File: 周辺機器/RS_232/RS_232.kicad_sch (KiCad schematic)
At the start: 16 parts, among them SW1 SW_DIP_x04, U1 CD74HC08, U10 74HC595, U11 74LS195, U2 CD74HC04, U3 4020, U4 4040, U5 74HC74, U6 74LS195, U7 74HC74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

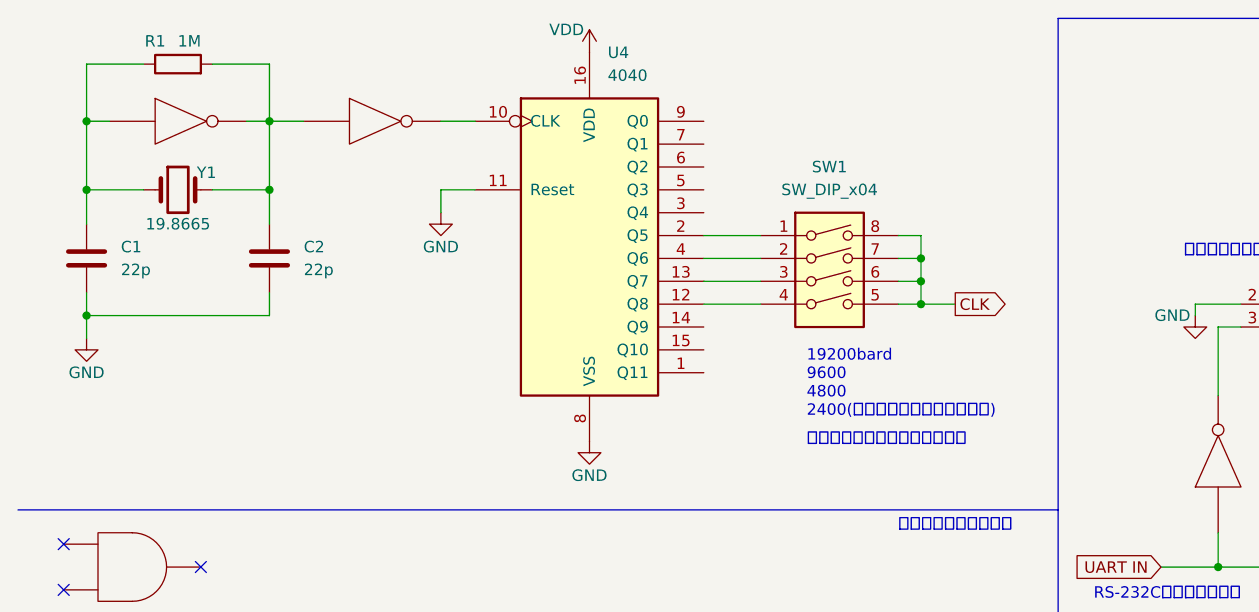
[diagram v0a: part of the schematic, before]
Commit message: 周辺機器RS-232C,定数および接続ピンの修正
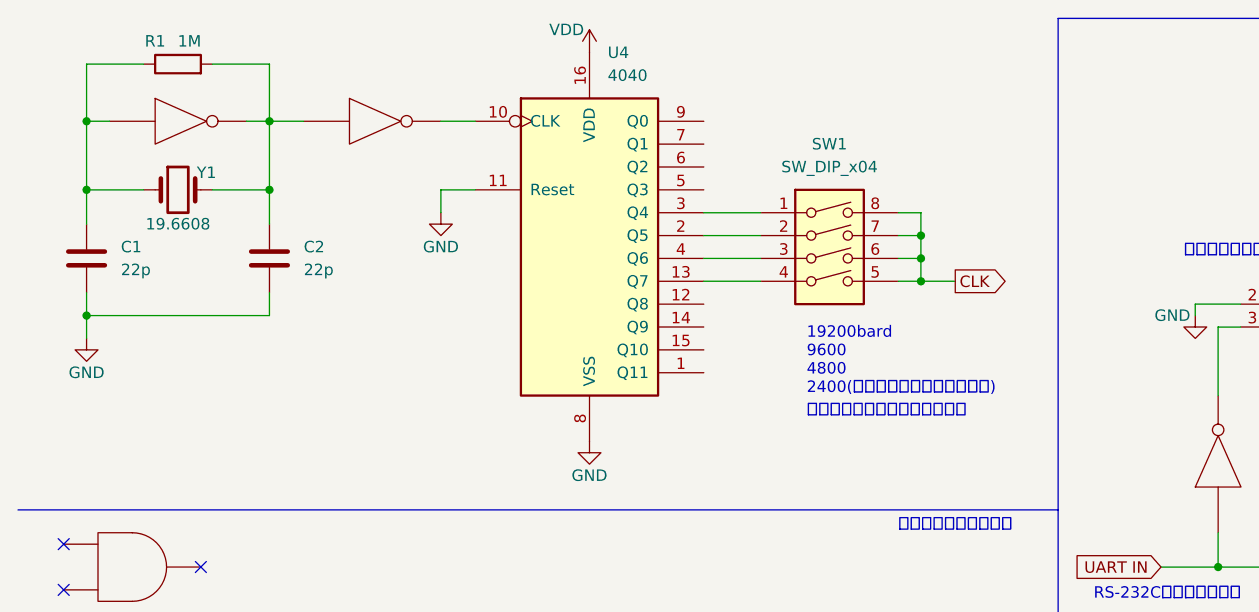
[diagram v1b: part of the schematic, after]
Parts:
- Y1: value 19.8665 -> 19.6608
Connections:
- net at SW1.1: now also U4.3 (Q4); no longer U4.2 (Q5)
- net at SW1.2: now also U4.2 (Q5); no longer U4.4 (Q6)
- net at SW1.3: now also U4.4 (Q6); no longer U4.13 (Q7)
- net at SW1.4: now also U4.13 (Q7); no longer U4.12 (Q8)
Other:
- moved on the sheet: SW1
